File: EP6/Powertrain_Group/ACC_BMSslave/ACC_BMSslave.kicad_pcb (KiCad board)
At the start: 4 copper layers, 100 x 79 mm, 275 parts, among them IC1 ADBMS1818ASWAZ-R7, IC10 NX2301P,215, IC11 NX2301P,215, IC12 NX2301P,215, IC13 NX2301P,215, IC14 NX2301P,215, IC15 NX2301P,215, IC16 NX2301P,215, IC17 NX2301P,215, IC2 LT8631IFE#PBF, IC3 NX2301P,215, IC4 NX2301P,215, IC5 NX2301P,215, IC6 NX2301P,215, IC7 NX2301P,215, IC8 NX2301P,215, IC9 NX2301P,215, J1 Cell taps A, J10 Cell taps B, J2 Temp probes A, J3 Temp probes B, J4 Temp probes C, J5 Temp probes D, J6 RJ45, J7 RJ45, J8 isoSPI_out, J9 isoSPI_in, U1 LM324DT, U2 ADG758CPZ, U3 ADG758CPZ, U4 ADG758CPZ, U5 ADG758CPZ

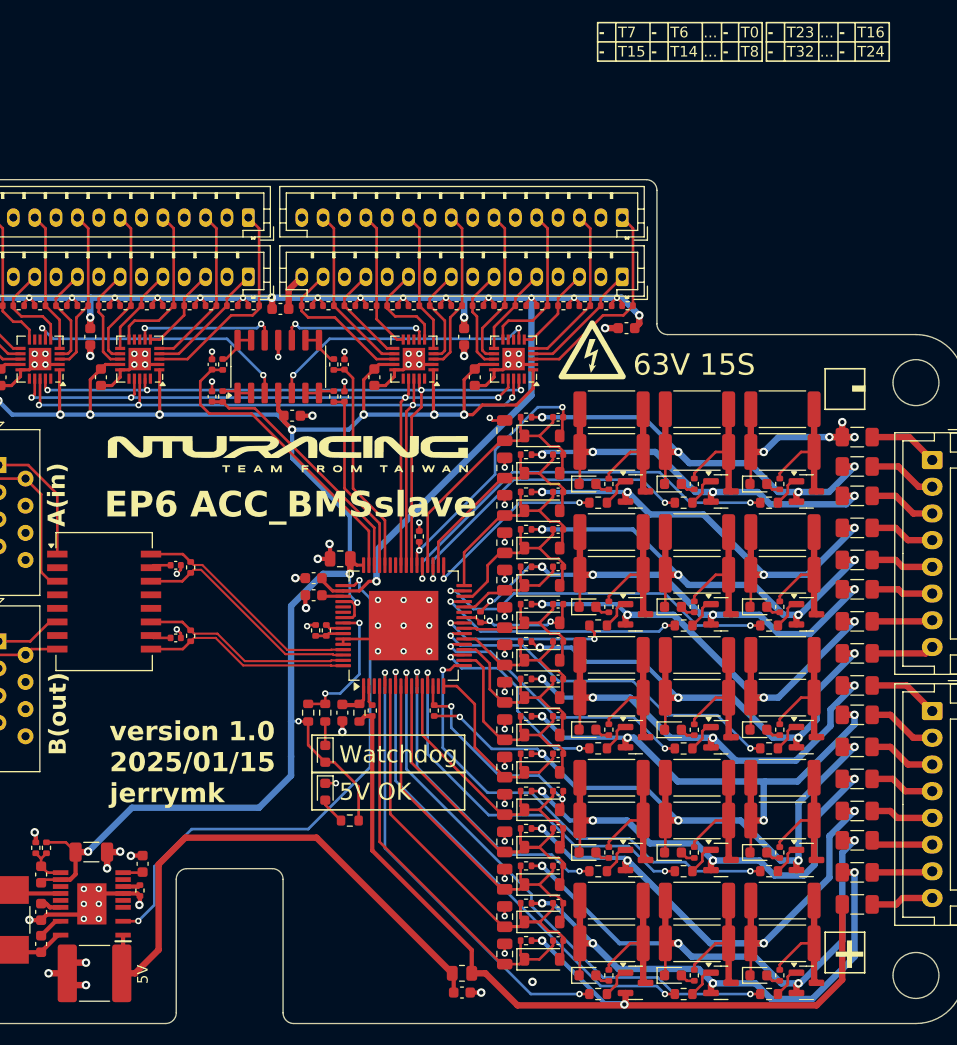
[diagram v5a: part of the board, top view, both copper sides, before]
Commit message: ACC_BMSslave optimise layout, added silk
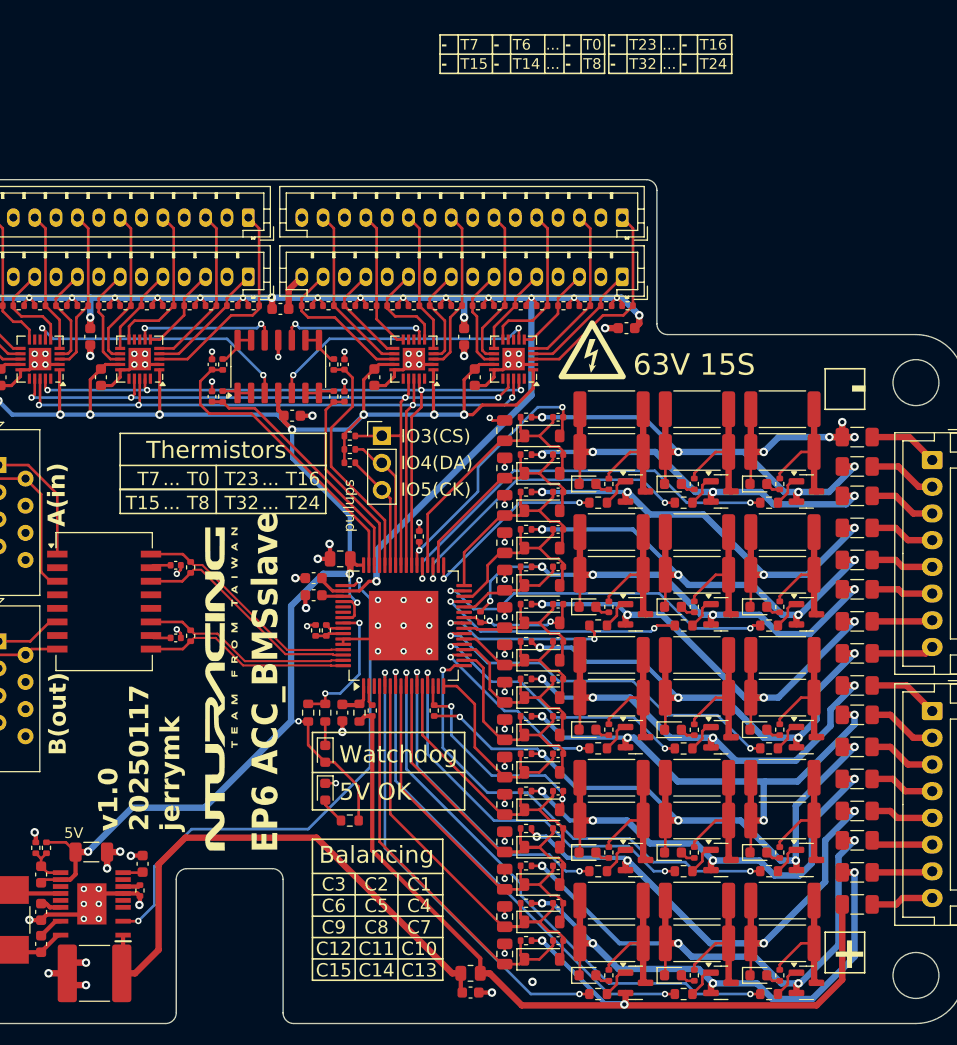
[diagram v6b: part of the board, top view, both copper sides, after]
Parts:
- added ? (x4): , Graphics, F.Cu at (72.0, 81.0)
- added ?: , Graphics, B.Cu at (72.0, 81.0)
- added J11: GPIO, Connector_PinHeader_2.54mm:PinHeader_1x03_P2.54mm_Vertical, F.Cu at (95.5, 74.5)
- added R128: 10k, Resistor_SMD:R_0402_1005Metric, F.Cu at (92.5, 74.5)
- added R129: 10k, Resistor_SMD:R_0402_1005Metric, F.Cu at (92.5, 75.8)
- added R130: 10k, Resistor_SMD:R_0402_1005Metric, F.Cu at (92.5, 77.0)
- moved ? 41.7 mm to (78.8, 115.2), turned to 90 degrees
- moved ? 2.12 mm to (72.0, 78.8) (x5)
- moved C5 0.80 mm to (103.8, 126.6)
- moved R33 0.80 mm to (103.8, 124.8)
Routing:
- net /GPIO4: track 0.00 -> 13.1 mm
- net /GPIO5: track 0.00 -> 10.9 mm
- net /GPIO3: track 67.4 -> 71.7 mm
- net VREG: track 190.1 -> 192.3 mm
- net /GPIO6: track 20.9 -> 22.5 mm
- net /S10: track 19.2 -> 17.9 mm
- net /CT5: track 52.5 -> 53.6 mm
- net /GPIO7: track 17.7 -> 18.7 mm
- net /CT12: track 53.5 -> 52.6 mm
- net /power/VIN: track 51.6 -> 52.4 mm
- net /C12: track 20.8 -> 21.6 mm
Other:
- board text added: "Balancing"
- board text added: "C1 C4 C7 C10 C13"
- board text added: "C2 C5 C8 C11 C14"
- board text added: "C3 C6 C9 C12 C15"
- board text added: "IO3(CS)"
- board text added: "IO4(DA)"
- board text added: "IO5(CK)"
- board text added: "TODO: Stitching vias"
- board text added: "Thermistors"
- board text added: "pullups"
- board text added: "v1.0 20250117 jerrymk"
- board text removed: "version 1.0 2025/01/15 jerrymk"
